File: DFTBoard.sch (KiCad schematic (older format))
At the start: 0 parts

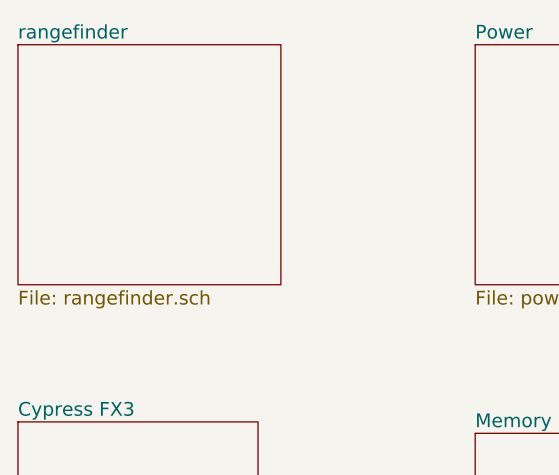
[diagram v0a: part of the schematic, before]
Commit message: encoders and headphone jack have been modified. many unconnections
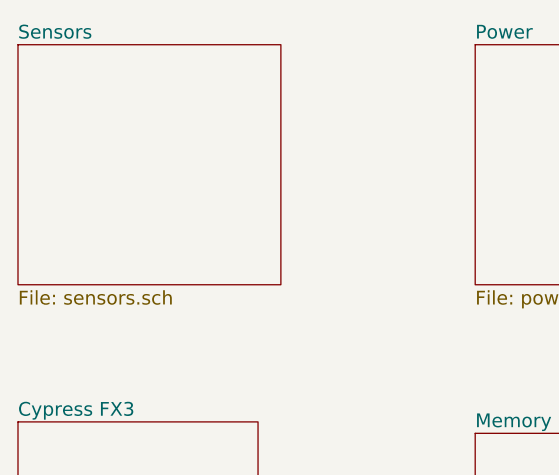
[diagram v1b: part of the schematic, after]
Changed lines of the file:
@@
 LIBS:DFTCustom
 LIBS:TLV320AIC3104
+LIBS:tpa2010d1
+LIBS:lis2hh12
+LIBS:Ghost
+LIBS:asflmb
+LIBS:er-con06hb-1
+LIBS:jack_trs_4pins
 EELAYER 25 0
 EELAYER END
@@
 S 1600 1950 1150 1050
 U 5852FF3B
-F0 "rangefinder" 60
-F1 "rangefinder.sch" 60
+F0 "Sensors" 60
+F1 "sensors.sch" 60
 $EndSheet
 $Sheet

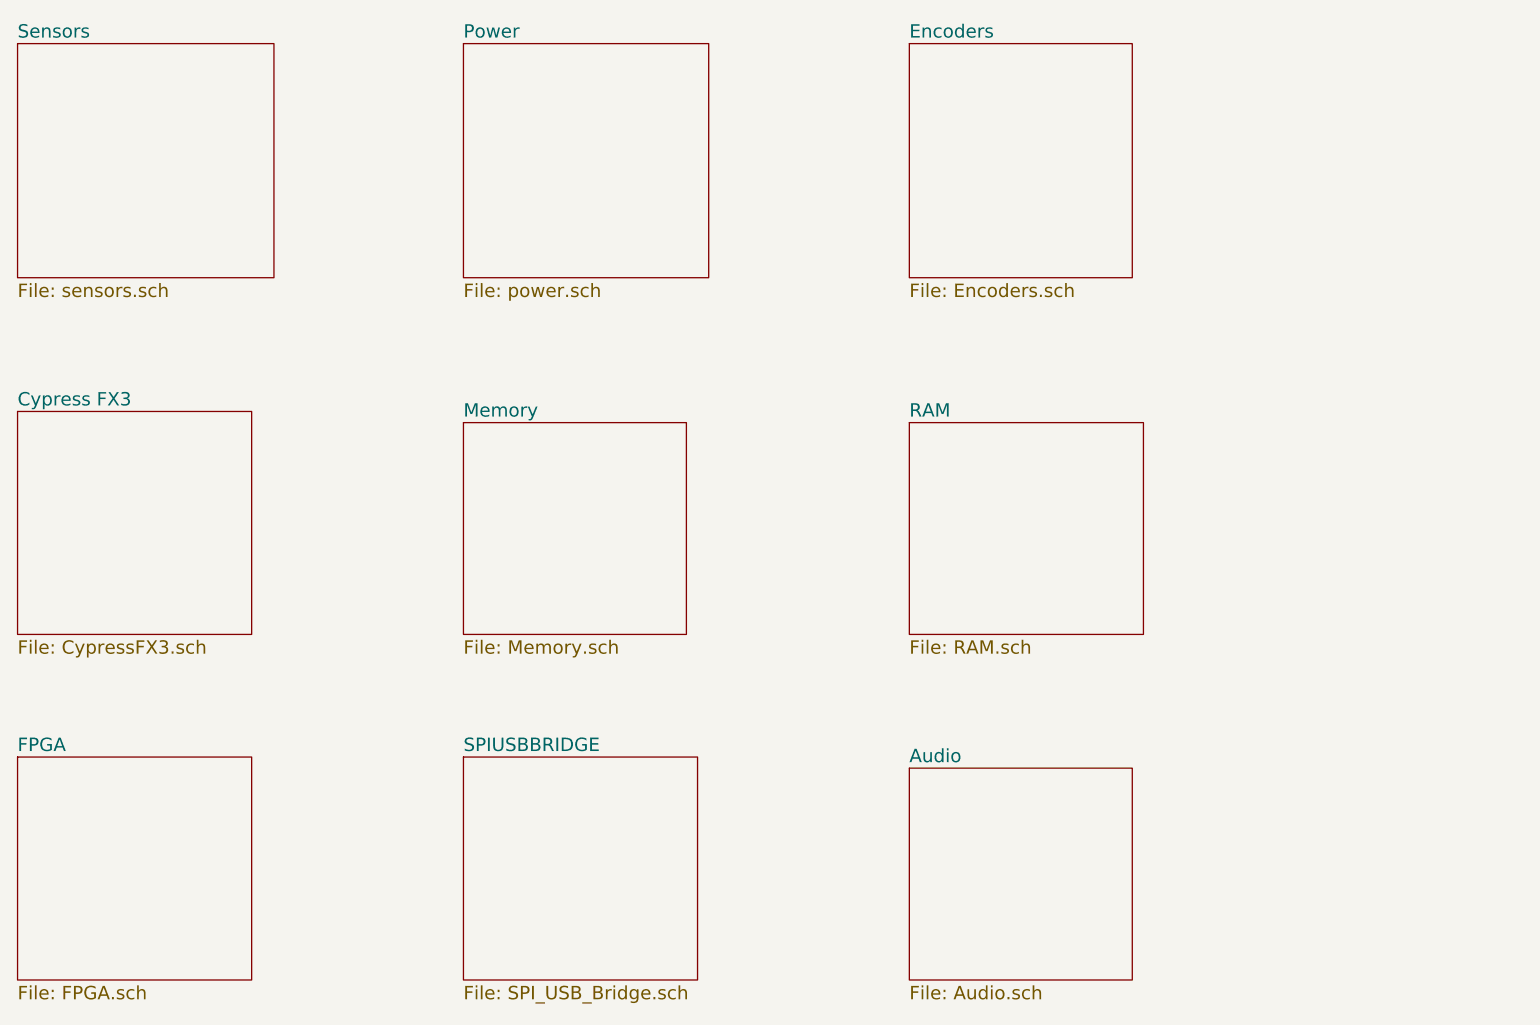
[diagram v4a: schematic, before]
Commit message: added caps to audio
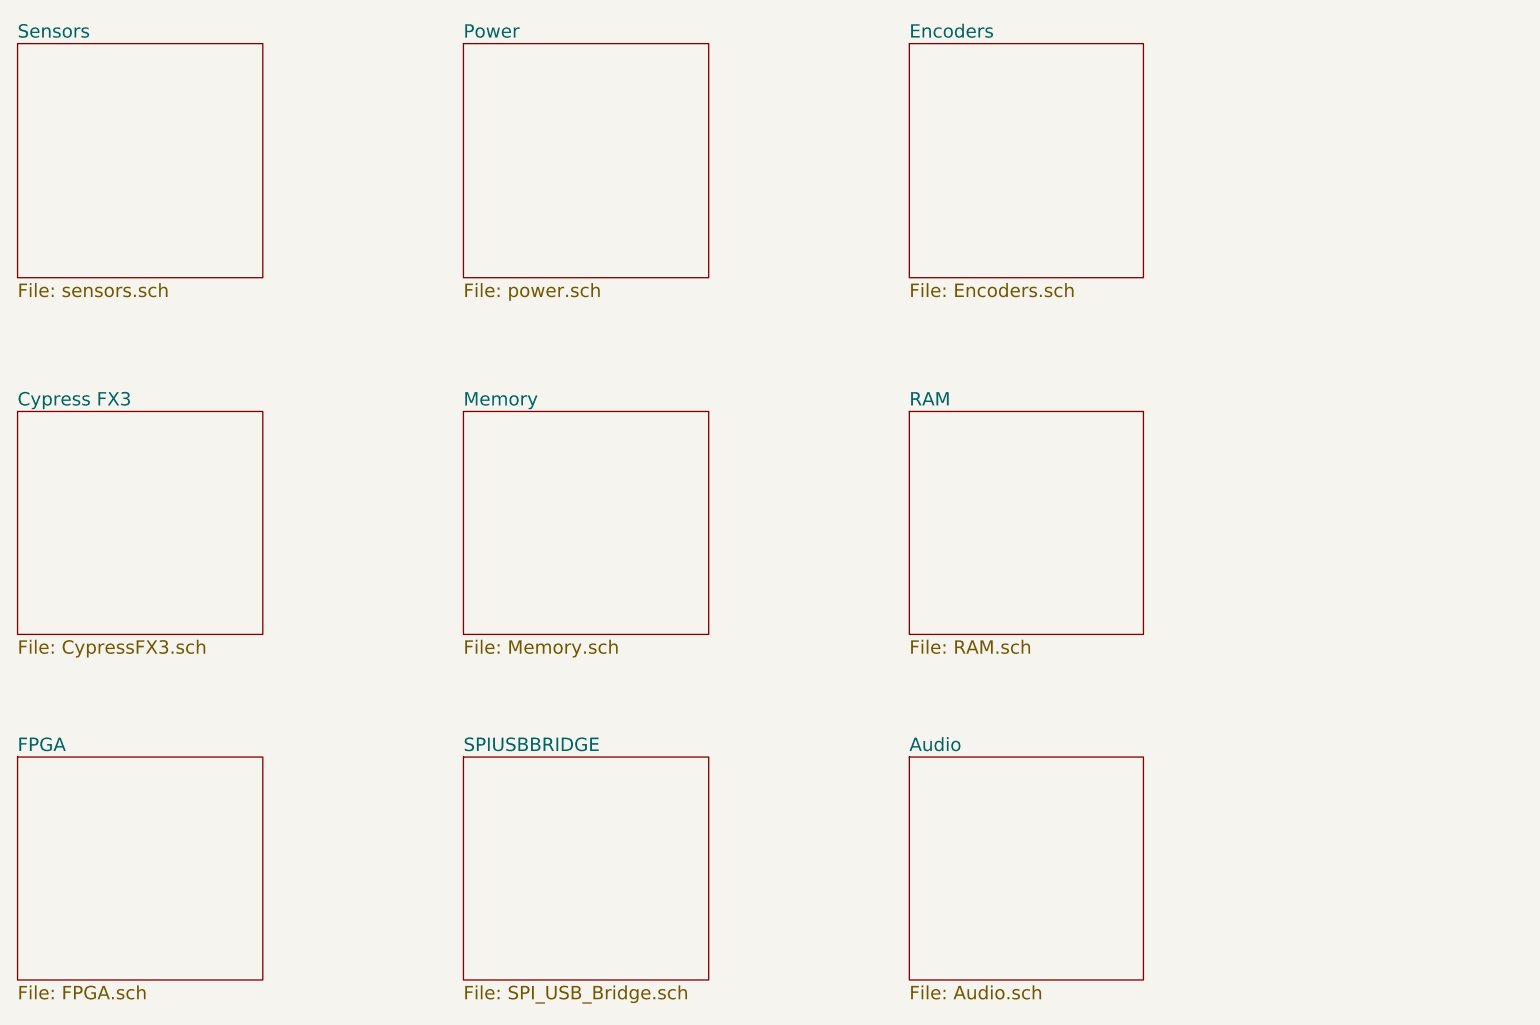
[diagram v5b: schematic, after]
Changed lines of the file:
@@
 $EndDescr
 $Sheet
-S 1600 5150 1050 1000
+S 1600 5150 1100 1000
 U 58508414
 F0 "FPGA" 60
@@
 $EndSheet
 $Sheet
-S 5600 5200 1000 950
+S 5600 5150 1050 1000
 U 58508444
 F0 "Audio" 60
@@
 $EndSheet
 $Sheet
-S 3600 3650 1000 950
+S 3600 3600 1100 1000
 U 58508456
 F0 "Memory" 60
@@
 $EndSheet
 $Sheet
-S 1600 3600 1050 1000
+S 1600 3600 1100 1000
 U 5852A88E
 F0 "Cypress FX3" 60
@@
 $EndSheet
 $Sheet
-S 1600 1950 1150 1050
+S 1600 1950 1100 1050
 U 5852FF3B
 F0 "Sensors" 60
@@
 $EndSheet
 $Sheet
-S 3600 5150 1050 1000
+S 3600 5150 1100 1000
 U 5862C4CE
 F0 "SPIUSBBRIDGE" 60
@@
 $EndSheet
 $Sheet
-S 5600 1950 1000 1050
+S 5600 1950 1050 1050
 U 586C33AF
 F0 "Encoders" 60
@@
 $EndSheet
 $Sheet
-S 5600 3650 1050 950
+S 5600 3600 1050 1000
 U 58818A06
 F0 "RAM" 60

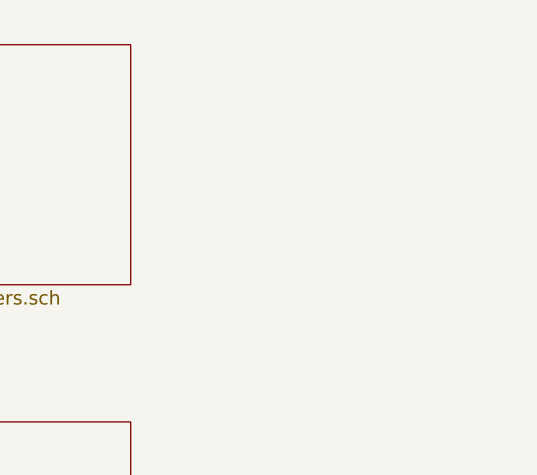
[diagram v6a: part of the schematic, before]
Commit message: about to resize all silkscreen text to 0.5
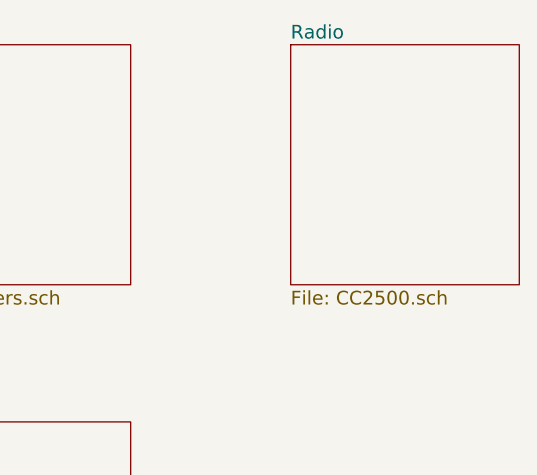
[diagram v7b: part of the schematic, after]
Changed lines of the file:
@@
 LIBS:er-con06hb-1
 LIBS:jack_trs_4pins
+LIBS:NorBot
+LIBS:CC2500
 EELAYER 25 0
 EELAYER END
 $Descr A4 11693 8268
 encoding utf-8
-Sheet 1 14
+Sheet 1 15
 Title ""
 Date ""
@@
 F1 "RAM.sch" 60
 $EndSheet
+$Sheet
+S 7350 1950 1000 1050
+U 5A36F1BB
+F0 "Radio" 60
+F1 "CC2500.sch" 60
+$EndSheet
 $EndSCHEMATC
